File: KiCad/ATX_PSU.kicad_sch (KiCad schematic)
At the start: 1 part

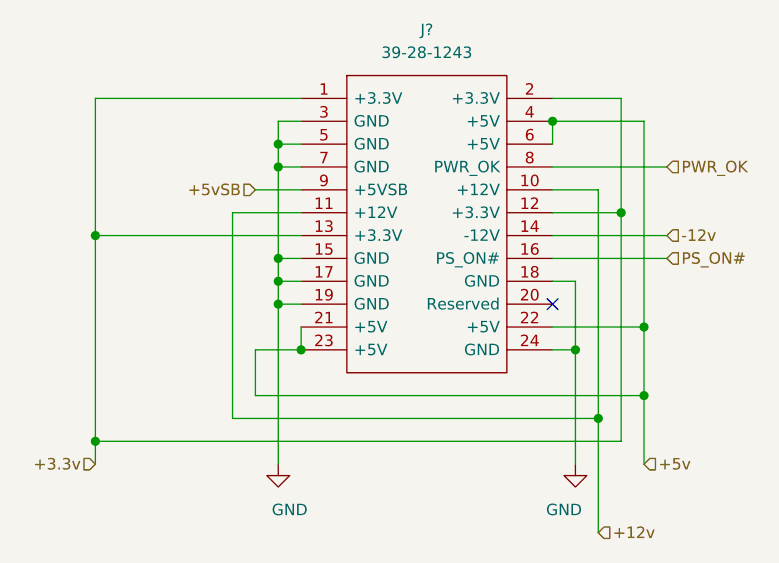
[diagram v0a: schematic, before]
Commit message: Big changes (see expanded comment)
Added new components:
USB2517-JZX USB2.0 Hub
SI-52100-002 Vertical USB2.0 A Header

Began work on USB schematic, mostly done. Needs power delivery work done
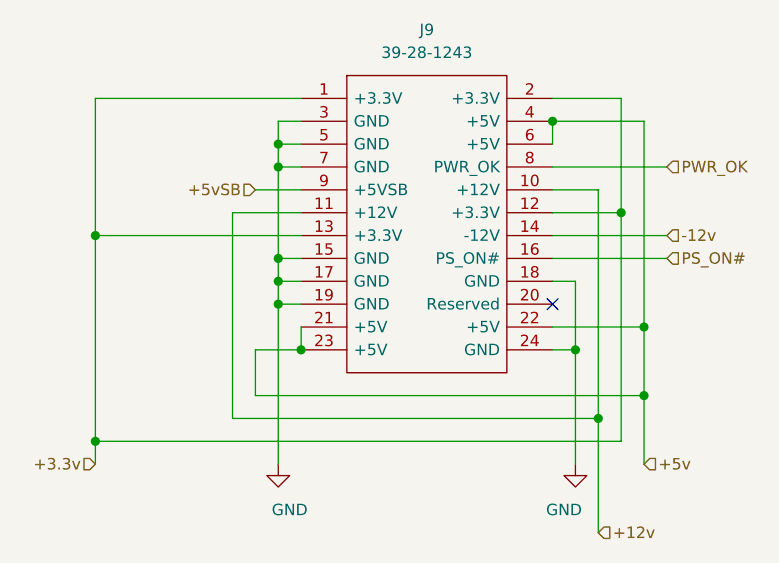
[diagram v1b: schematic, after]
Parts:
- gave numbers to parts that had none: 1
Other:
- company: (none) -> TheGuyDanish
- title: (none) -> 24-pin ATX Connector
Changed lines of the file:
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@@
 (kicad_sch (version 20200828) (generator eeschema)
-  (page 4 4)
+  (page 5 5)
   (paper "A4")
+  (title_block
+    (title "24-pin ATX Connector")
+    (date "2020-11-14")
+    (rev "0.1")
+    (company "TheGuyDanish")
+    (comment 1 "https://github.com/theguydanish/cm4_matx")
+  )
   (junction (at 121.92 91.44) (diameter 1.016) (color 0 0 0 0))
   (junction (at 121.92 114.3) (diameter 1.016) (color 0 0 0 0))
@@
     (stroke (width 0) (type solid) (color 0 0 0 0))
   )
-  (wire (pts (xy 137.16 111.76) (xy 172.72 111.76))
+  (wire (pts (xy 137.16 111.76) (xy 177.8 111.76))
     (stroke (width 0) (type solid) (color 0 0 0 0))
   )
@@
     (stroke (width 0) (type solid) (color 0 0 0 0))
   )
-  (wire (pts (xy 139.7 109.22) (xy 144.78 109.22))
+  (wire (pts (xy 139.7 109.22) (xy 182.88 109.22))
     (stroke (width 0) (type solid) (color 0 0 0 0))
   )
@@
     (stroke (width 0) (type solid) (color 0 0 0 0))
   )
-  (wire (pts (xy 144.78 109.22) (xy 182.88 109.22))
-    (stroke (width 0) (type solid) (color 0 0 0 0))
-  )
   (wire (pts (xy 172.72 76.2) (xy 180.34 76.2))
     (stroke (width 0) (type solid) (color 0 0 0 0))
@@
   )
   (wire (pts (xy 172.72 104.14) (xy 175.26 104.14))
-    (stroke (width 0) (type solid) (color 0 0 0 0))
-  )
-  (wire (pts (xy 172.72 111.76) (xy 177.8 111.76))
     (stroke (width 0) (type solid) (color 0 0 0 0))
   )
@@
   (symbol (lib_id "power:GND") (at 142.24 116.84 0) (unit 1)
     (in_bom yes) (on_board yes)
-    (property "Reference" "#PWR?" (id 0) (at 142.24 123.19 0)
+    (property "Reference" "#PWR0123" (id 0) (at 142.24 123.19 0)
       (effects (font (size 1.27 1.27)) hide)
     )
@@
   (symbol (lib_id "power:GND") (at 175.26 116.84 0) (unit 1)
     (in_bom yes) (on_board yes)
-    (property "Reference" "#PWR?" (id 0) (at 175.26 123.19 0)
+    (property "Reference" "#PWR0124" (id 0) (at 175.26 123.19 0)
       (effects (font (size 1.27 1.27)) hide)
     )
@@
   (symbol (lib_id "CM4_MATX:39-28-1243") (at 144.78 76.2 0) (unit 1)
     (in_bom yes) (on_board yes)
-    (property "Reference" "J?" (id 0) (at 158.75 68.58 0))
+    (property "Reference" "J9" (id 0) (at 158.75 68.58 0))
     (property "Value" "39-28-1243" (id 1) (at 158.75 71.12 0))
     (property "Footprint" "SHDR24W125P550X420_2X12_5160X960X1310P" (id 2) (at 135.89 50.8 0)
